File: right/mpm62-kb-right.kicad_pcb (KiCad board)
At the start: 2 copper layers, 161.9 x 95.2 mm, 72 parts, among them J1 Conn_01x04_Male, SW1 SW_Push, U1 MCP23018-E_SP

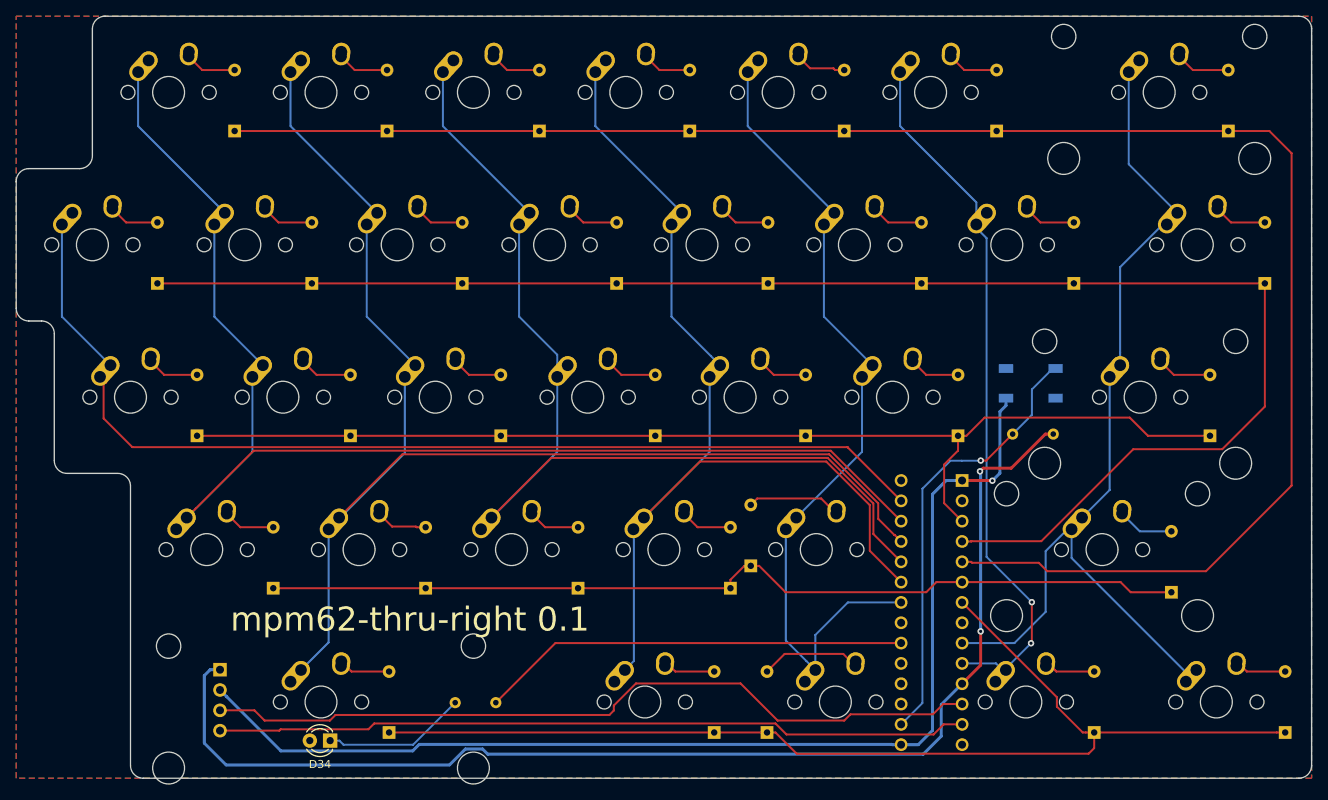
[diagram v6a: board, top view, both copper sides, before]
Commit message: Fix some small components in path of stabilizers.
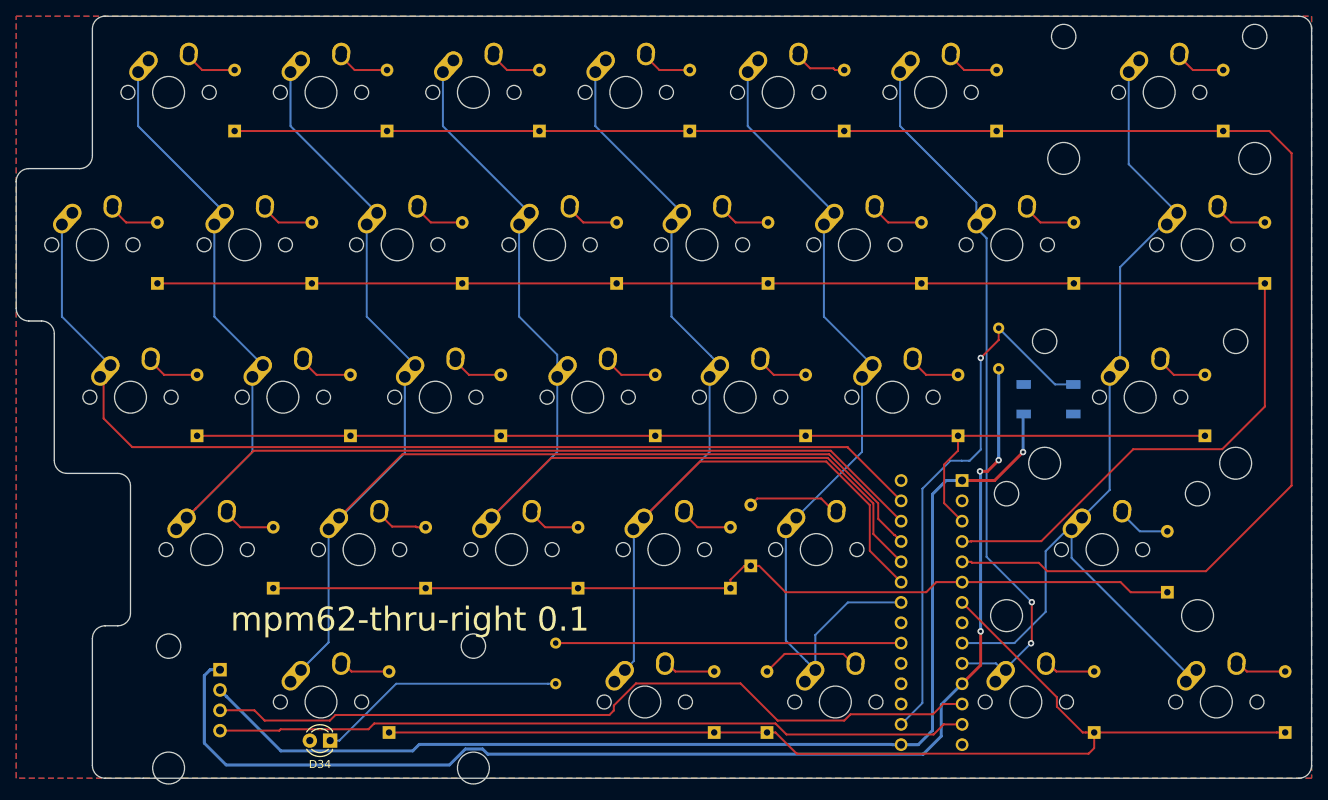
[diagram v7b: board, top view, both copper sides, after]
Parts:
- moved R2 10.6 mm to (170.4, 91.7), turned to 90 degrees
- moved R1 10.6 mm to (115.1, 126.0), turned to 270 degrees
- moved SW1 2.97 mm to (176.7, 95.5)
- moved D29 0.63 mm to (198.5, 62.0)
- moved D31 0.63 mm to (196.2, 100.1)
- moved D32 0.51 mm to (191.5, 119.6)
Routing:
- net Net-(D34-Pad1): track 18.0 -> 31.1 mm
- net Net-(R2-Pad2): track 55.3 -> 68.2 mm
- net Net-(R1-Pad1): track 53.7 -> 43.2 mm
- net VCC: track 152.2 -> 155.5 mm, vias 2 -> 3
- net ROW2: track 140.8 -> 138.9 mm
- net GND: track 142.1 -> 141.1 mm
- net Net-(D29-Pad2): track 6.84 -> 6.21 mm
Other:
- outline, holes or cut-outs redrawn
